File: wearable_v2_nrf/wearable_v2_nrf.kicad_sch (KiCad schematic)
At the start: 52 parts, among them IC1 MCP73831T-2ACI_OT, J1 Conn_01x04, J2 217175-0001, J3 Conn_01x03, M1 Motor_DC, Q1 PMOS, Q2 NPN, SW1 Reset, U1 nRF52811-QCxx, U3 BMI270, U4 MCP1700x-330xxMB, U5 2450AT18A100E, Y1 ABM10W-32.0000MHZ-8-B1U-T3, Y2 Crystal

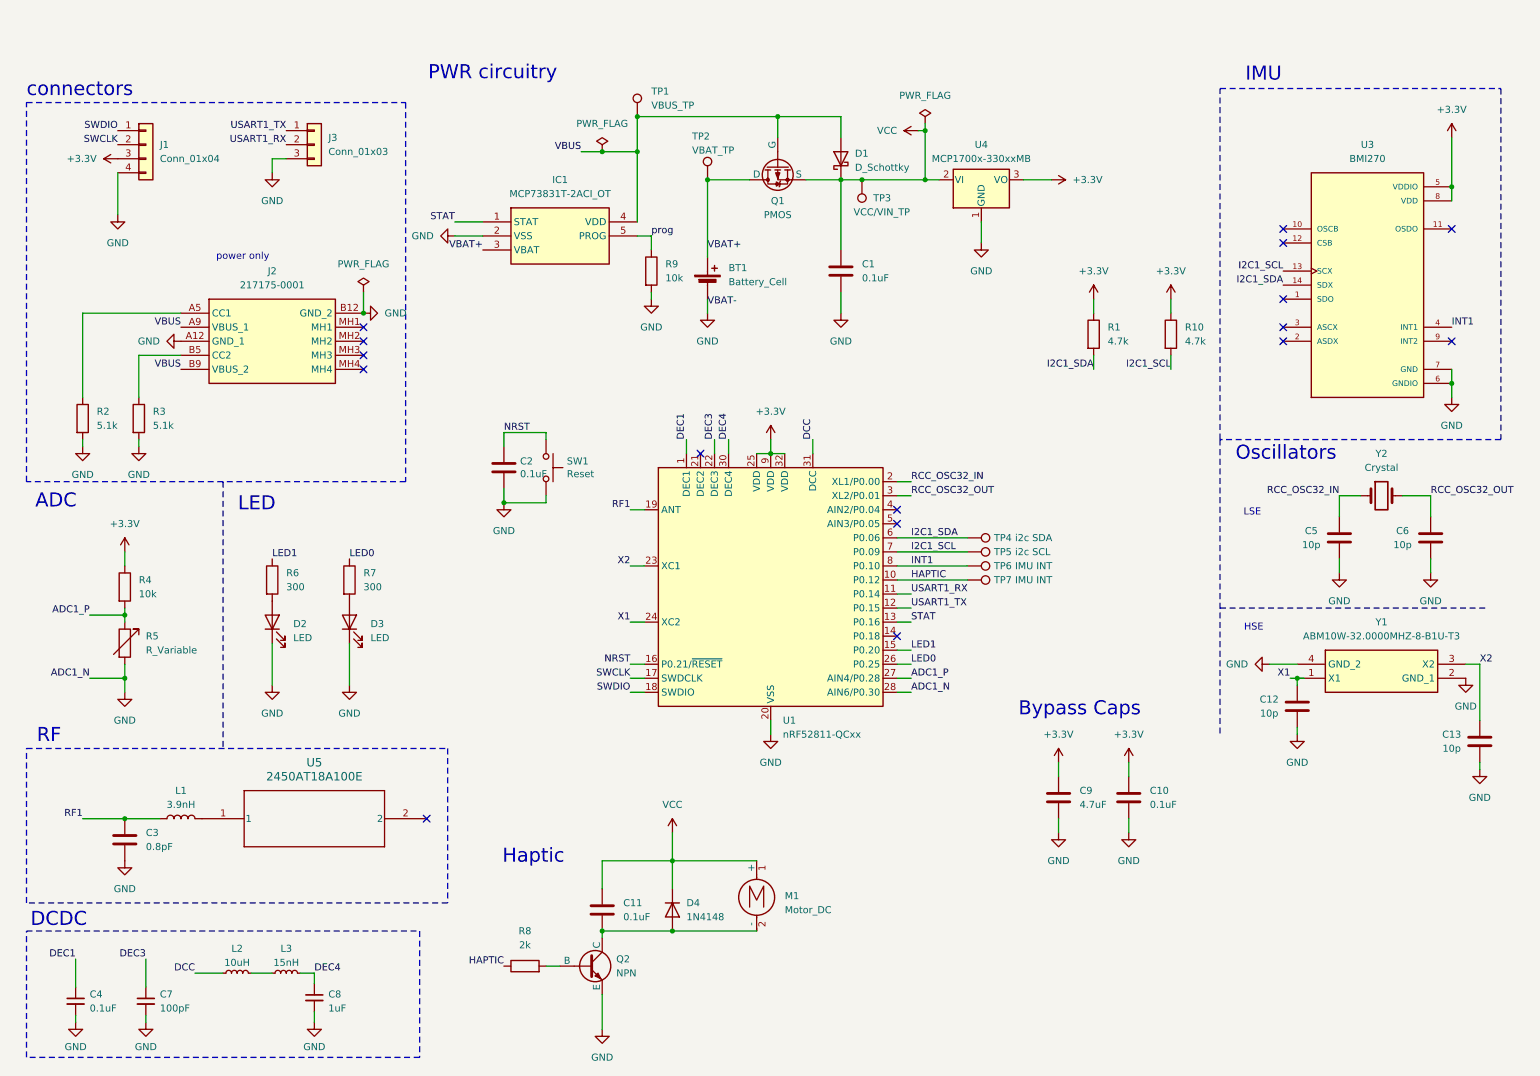
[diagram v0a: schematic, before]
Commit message: changes
fixed mosfet symbol-footprint,
connection jst->molex pico,
made HSC closer
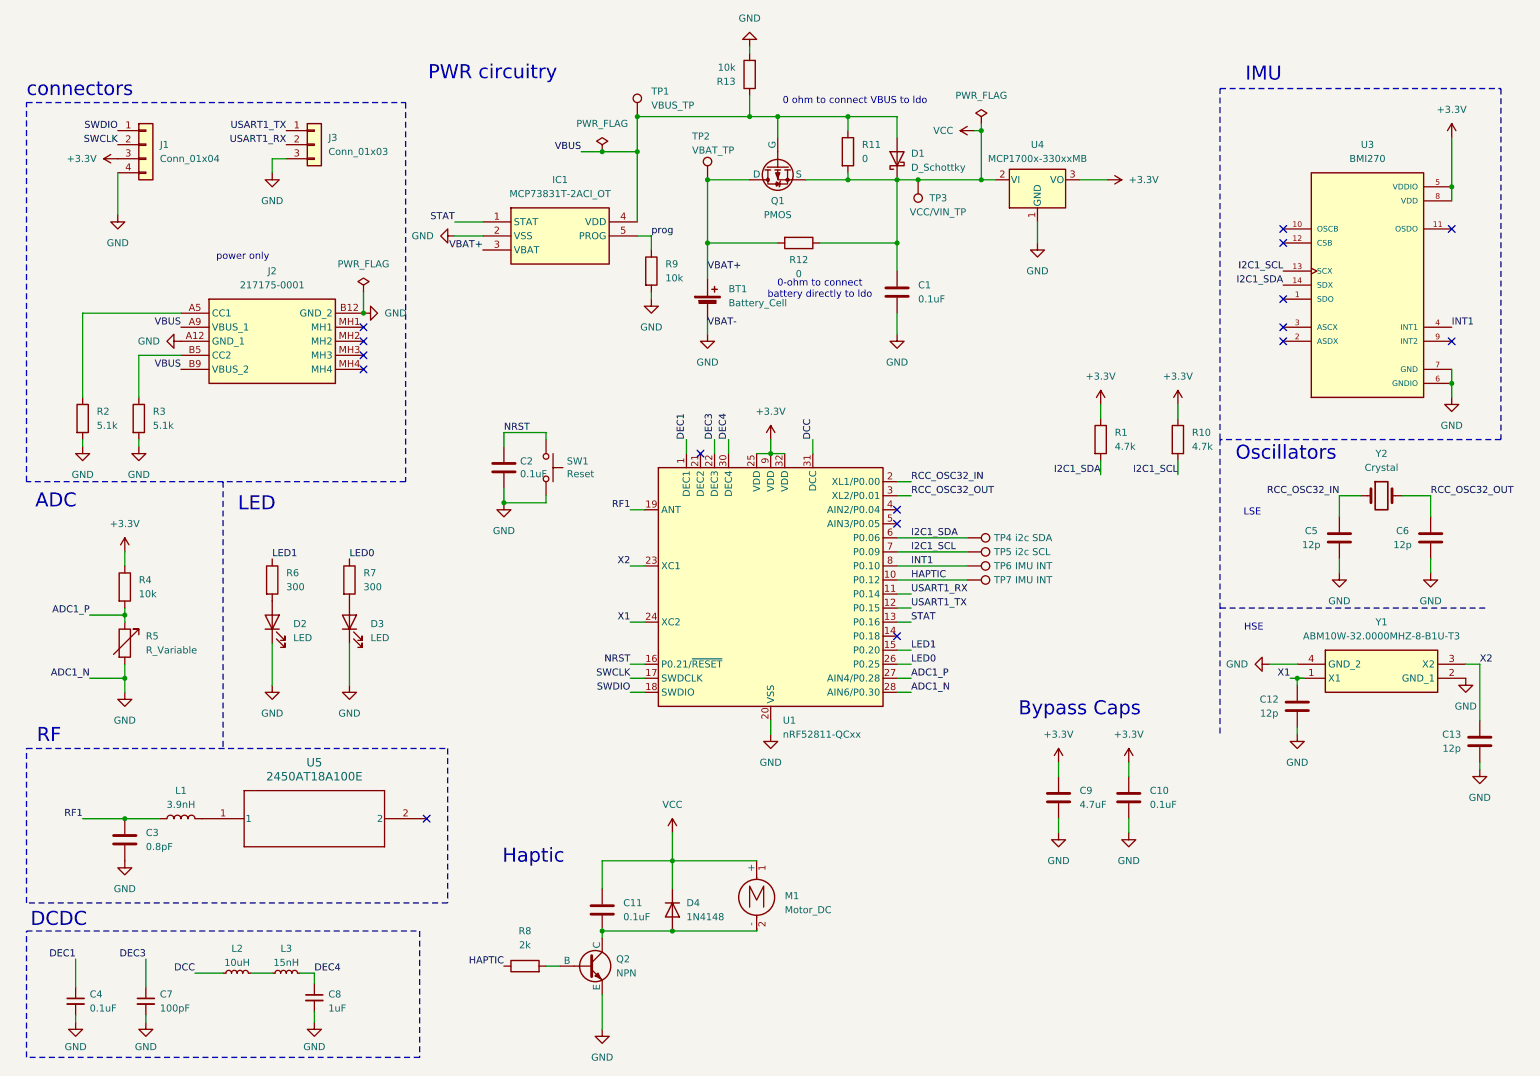
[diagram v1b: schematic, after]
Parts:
- added R11, R12: 0, Resistor_SMD:R_0805_2012Metric, symbol Device:R
- added R13: 10k, Resistor_SMD:R_0805_2012Metric, symbol Device:R
- BT1: footprint Connector_JST:JST_PH_B2B-PH-K_1x02_P2.00mm_Vertical -> Connector_Molex:Molex_PicoBlade_53047-0210_1x02_P1.25mm_Vertical
- C12, C13, C5, C6: value 10p -> 12p
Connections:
- net GND: now also R13.2
- net VBAT+: now also Q1.3 (D), R12.2; no longer Q1.1 (D)
- net VBUS: now also Q1.1 (G), R11.1, R13.1; no longer Q1.2 (G)
- net VCC: now also Q1.2 (S), R11.2, R12.1; no longer Q1.3 (S)
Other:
- note added: "0 ohm to connect VBUS to ldo"
- note added: "0-ohm to connect battery directly to ldo"
- moved on the sheet: BT1, C1, D1, R1, R10, TP3, U4

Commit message: v2 revisions for nrf pcb
fix imu, fix adc
includes new firmware for nrf52811
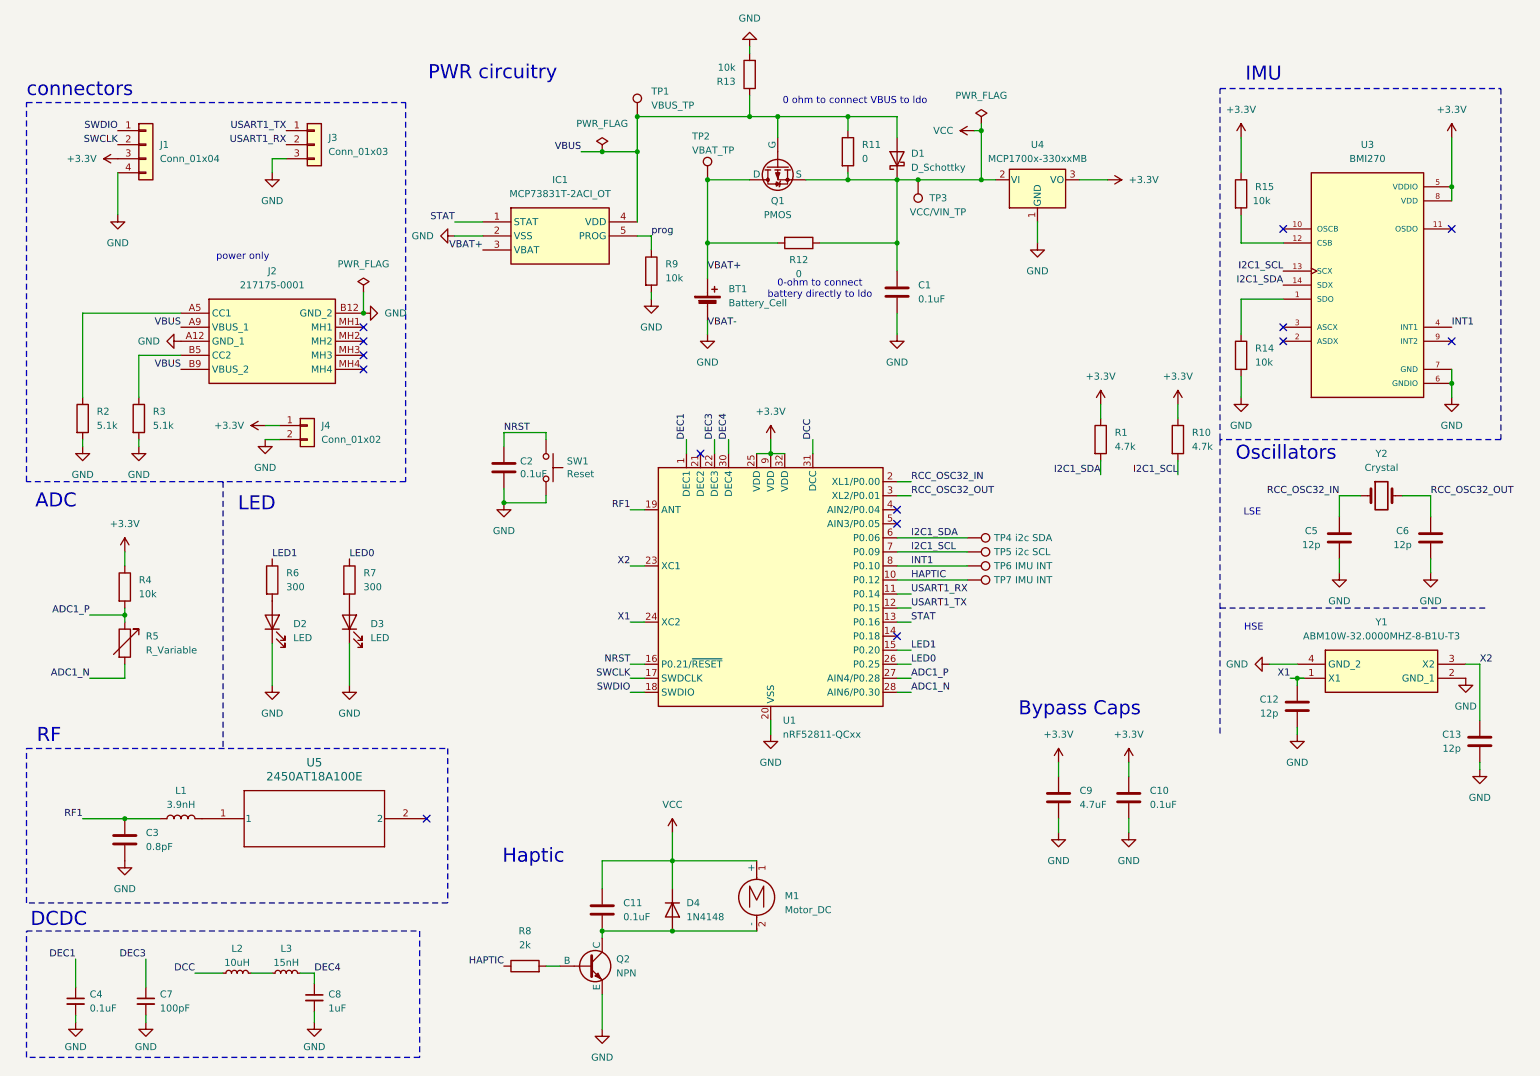
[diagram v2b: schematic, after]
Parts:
- added J4: Conn_01x02, Connector_PinHeader_2.54mm:PinHeader_1x02_P2.54mm_Vertical, symbol Connector_Generic:Conn_01x02
- added R14, R15: 10k, Resistor_SMD:R_0805_2012Metric, symbol Device:R
- R5: footprint Connector_PinSocket_2.54mm:PinSocket_1x02_P2.54mm_Horizontal -> Connector_PinHeader_2.54mm:PinHeader_1x02_P2.54mm_Vertical
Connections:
- net +3.3V: now also J4.1 (Pin_1), R15.1
- net GND: now also J4.2 (Pin_2), R14.2; no longer R5.2, U1.28 (AIN6/P0.30)
- net at U3.1 (SDO): now also R14.1
- net at U3.12 (CSB): now also R15.2
- new net ADC1_N: R5.2, U1.28 (AIN6/P0.30)
- no-connect marks 16 -> 14

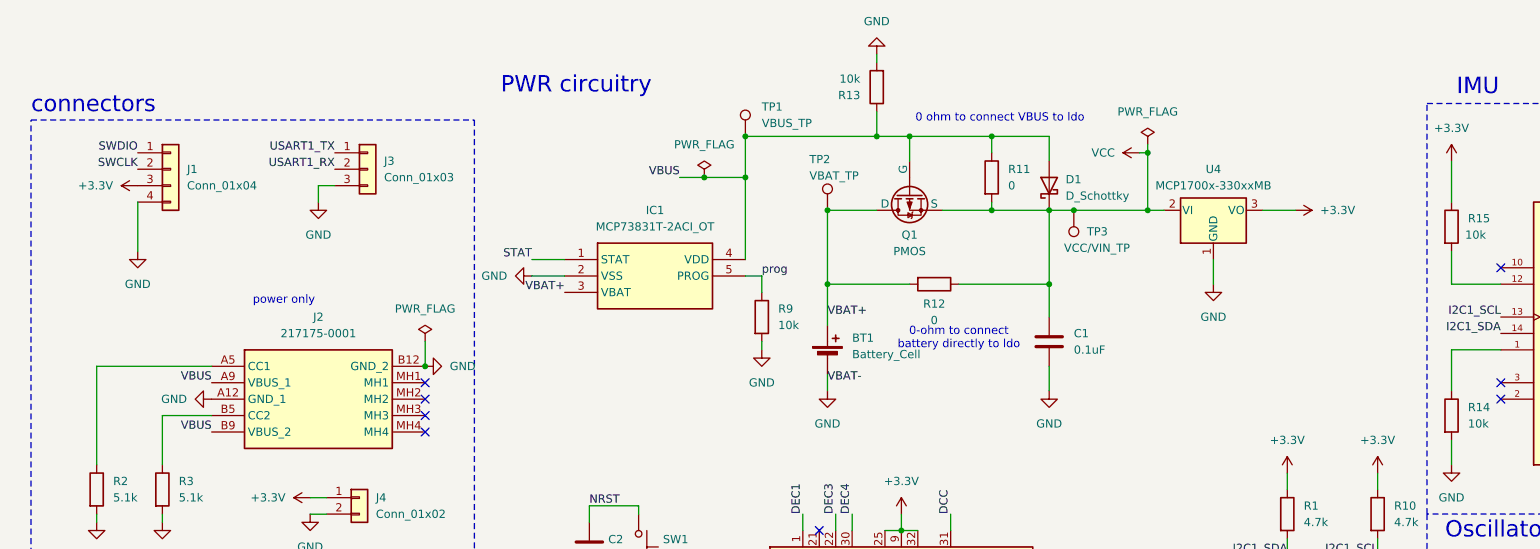
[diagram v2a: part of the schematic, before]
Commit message: final nrf board edits + ble sniffer py script
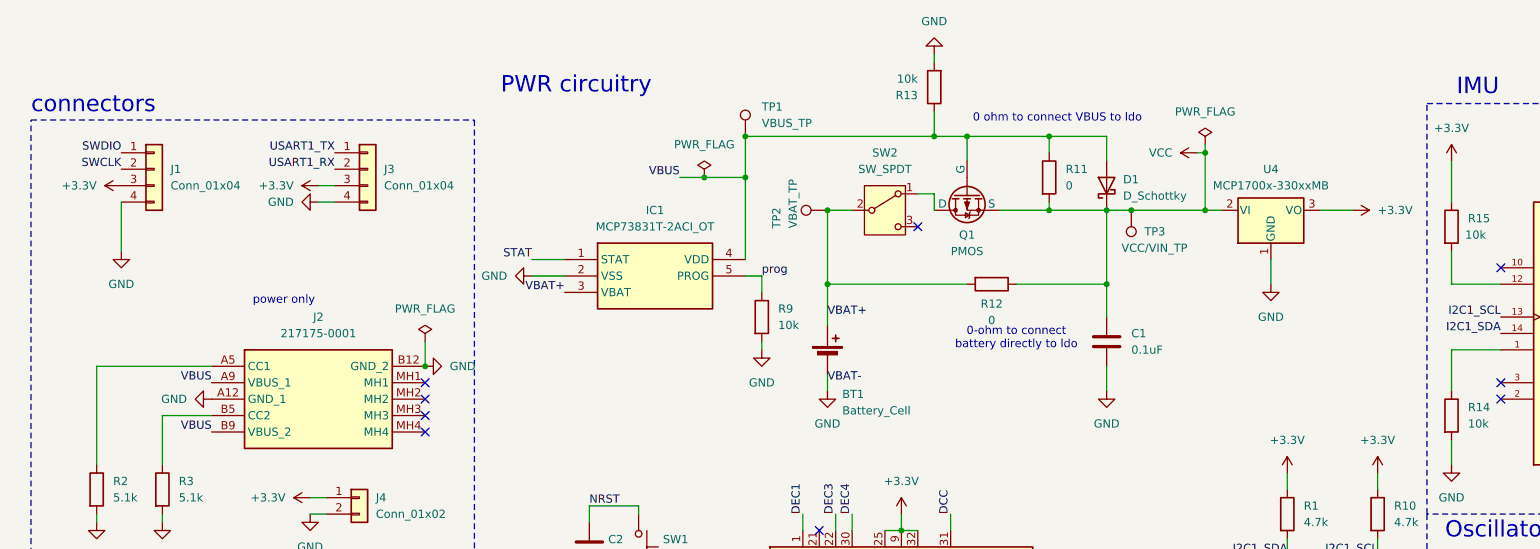
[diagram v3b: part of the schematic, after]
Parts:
- removed J3: Conn_01x03, Connector_PinHeader_2.54mm:PinHeader_1x03_P2.54mm_Vertical, symbol Connector_Generic:Conn_01x03
- added J3: Conn_01x04, Connector_PinHeader_2.54mm:PinHeader_1x04_P2.54mm_Vertical, symbol Connector_Generic:Conn_01x04
- added SW2: SW_SPDT, Connector_PinHeader_2.54mm:PinHeader_1x03_P2.54mm_Vertical, symbol Switch:SW_SPDT
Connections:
- net +3.3V: now also J3.3 (Pin_3)
- net GND: now also J3.4 (Pin_4)
- net USART1_RX: now also J3.2 (Pin_2)
- net USART1_TX: now also J3.1 (Pin_1)
- net VBAT+: now also SW2.2 (B); no longer Q1.3 (D)
- new net: Q1.3 (D), SW2.1 (A)
- no-connect marks 14 -> 15
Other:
- moved on the sheet: C1, D1, J1, Q1, R11, R12, R13, TP2, TP3, U4

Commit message: final pcb design :)
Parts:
- added R16: 0, Resistor_SMD:R_0805_2012Metric, symbol Device:R
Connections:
- net STAT: now also R16.1; no longer IC1.1 (STAT)
- new net: IC1.1 (STAT), R16.2
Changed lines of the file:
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@@
+	(wire
+		(pts
+			(xy 92.71 35.56) (xy 92.71 36.83)
+		)
+		(stroke
+			(width 0)
+			(type default)
+		)
+	)
 	(wire
 		(pts
@@
 		)
 	)
-	(label "STAT"
-		(at 92.71 44.45 180)
-		(fields_autoplaced yes)
-		(effects
-			(font
-				(size 1.27 1.27)
-			)
-			(justify right bottom)
-		)
-	)
 	(label "DCC"
 		(at 157.48 83.82 90)
@@
 			)
 			(justify left bottom)
+		)
+	)
+	(label "STAT"
+		(at 92.71 35.56 180)
+		(fields_autoplaced yes)
+		(effects
+			(font
+				(size 1.27 1.27)
+			)
+			(justify right bottom)
 		)
 	)
@@
 					(unit 1)
 				)
+			)
+		)
+	)
+	(symbol
+		(lib_id "Device:R")
+		(at 92.71 40.64 0)
+		(unit 1)
+		(exclude_from_sim no)
+		(in_bom yes)
+		(on_board yes)
+		(dnp no)
+		(property "Reference" "R16"
+			(at 95.758 40.64 90)
+			(effects
+				(font
+					(size 1.27 1.27)
+				)
+			)
+		)
+		(property "Value" "0"
+			(at 98.298 40.64 90)
+			(effects
+				(font
+					(size 1.27 1.27)
+				)
+			)
+		)
+		(property "Footprint" "Resistor_SMD:R_0805_2012Metric"
+			(at 90.932 40.64 90)
+			(effects
+				(font
+					(size 1.27 1.27)
+				)
+				(hide yes)
+			)
+		)
+		(property "Datasheet" "~"
+			(at 92.71 40.64 0)
+			(effects
+				(font
+					(size 1.27 1.27)
+				)
+				(hide yes)
+			)
+		)
+		(property "Description" "Resistor"
+			(at 92.71 40.64 0)
+			(effects
+				(font
+					(size 1.27 1.27)
+				)
+				(hide yes)
+			)
+		)
+		(pin "2"
+		)
+		(pin "1"
+		)
+		(instances
+			(project "wearable_v2_nrf"
+				(path "/04076b6c-00f0-4736-97bb-31ddf474c7f4"
+					(reference "R16")
+					(unit 1)
+				)
